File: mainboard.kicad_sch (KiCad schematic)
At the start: 0 parts

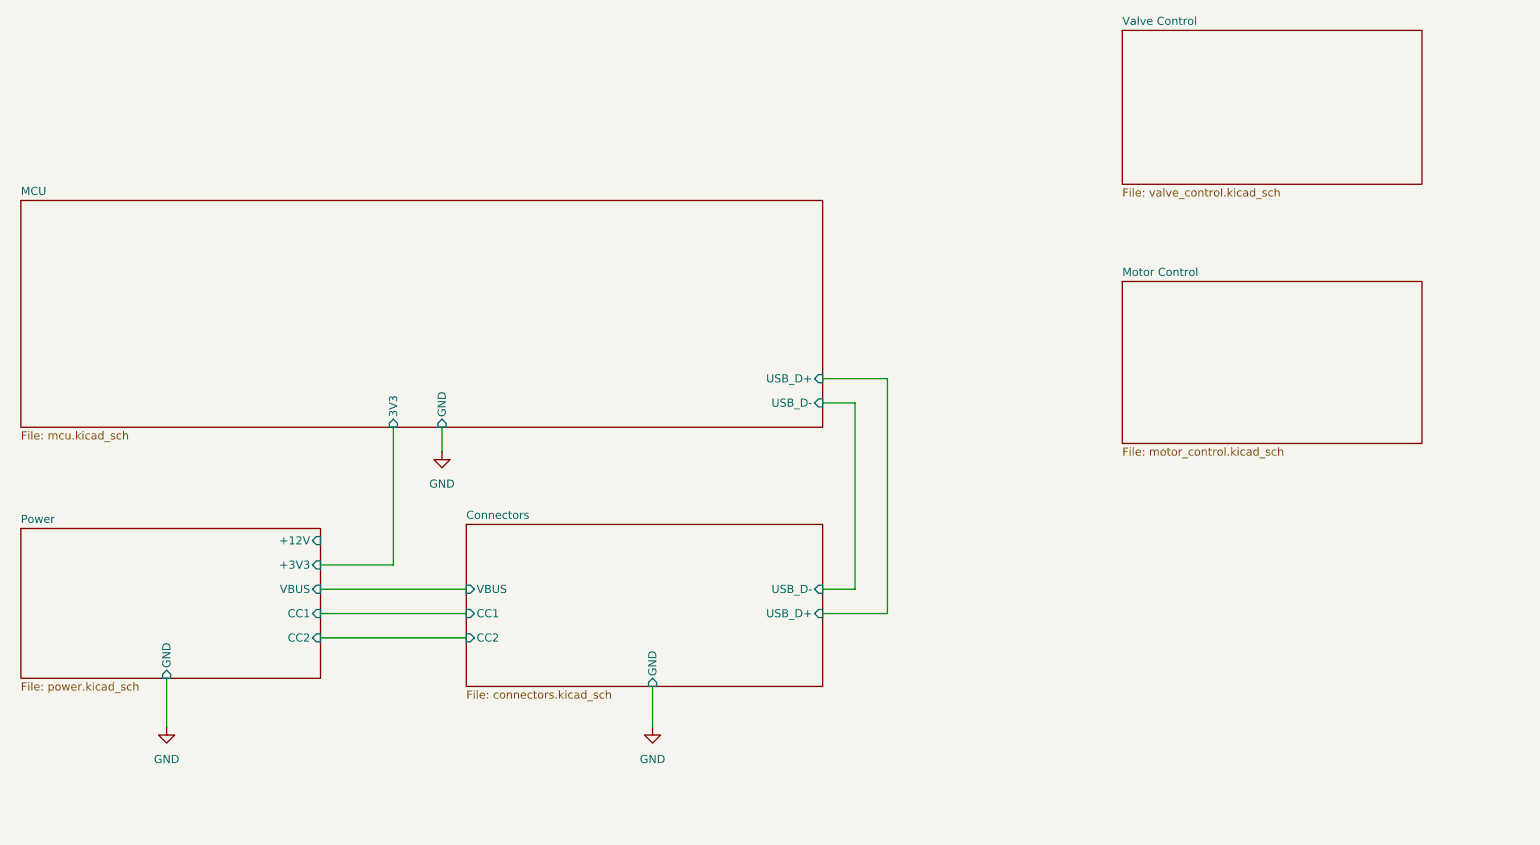
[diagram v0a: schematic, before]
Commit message: Add ESP32-S3-WROOM-1, 5V rail and UI sheet
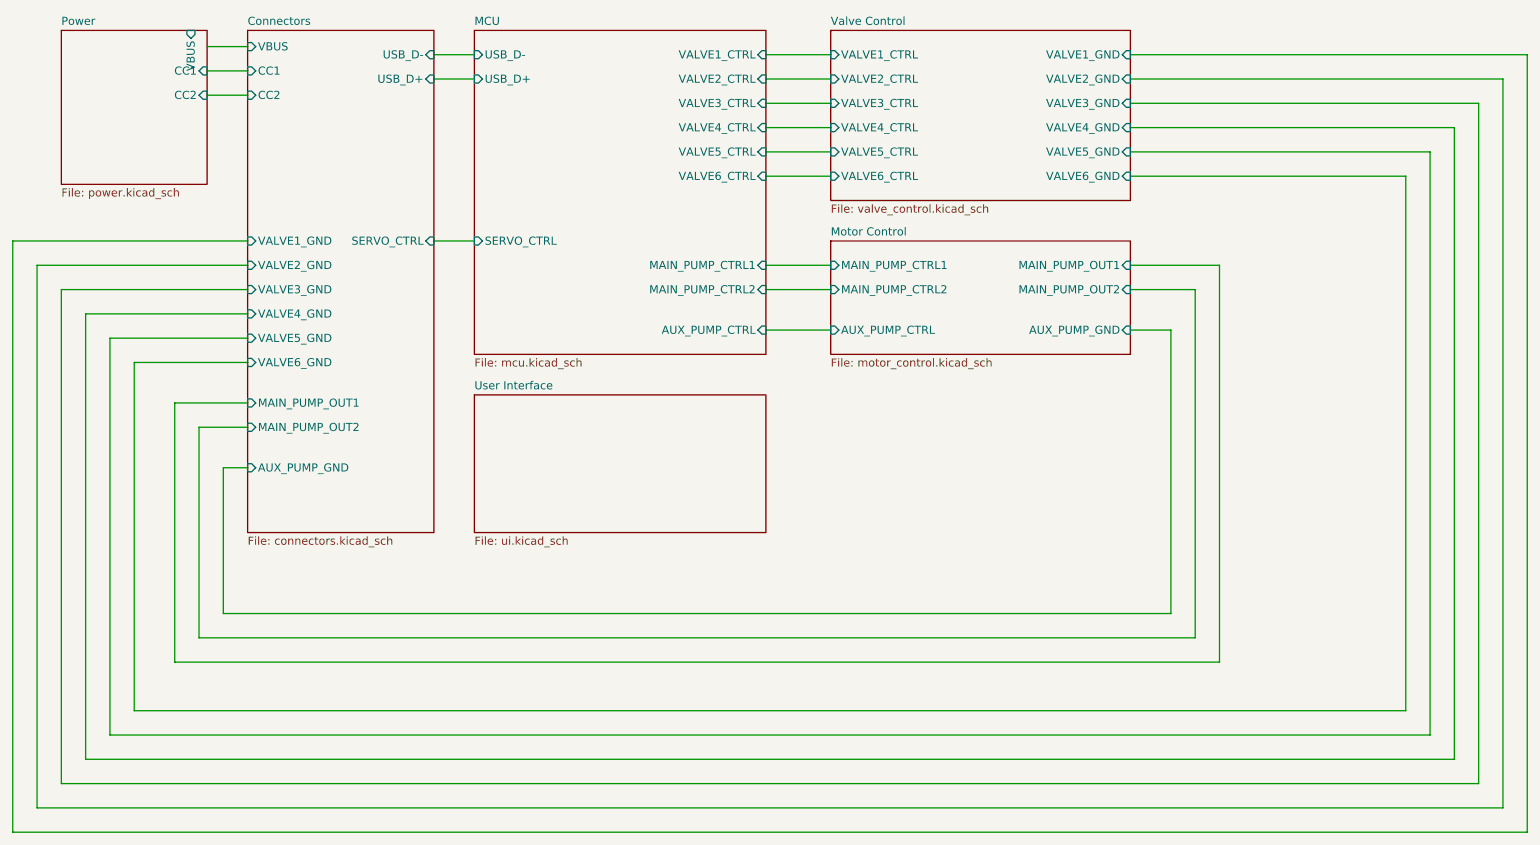
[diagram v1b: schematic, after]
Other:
- added sheet User Interface (ui.kicad_sch)
- sheet Connectors ports: added AUX_PUMP_GND, MAIN_PUMP_OUT1, MAIN_PUMP_OUT2, SERVO_CTRL, VALVE1_GND, VALVE2_GND, VALVE3_GND, VALVE4_GND, VALVE5_GND, VALVE6_GND; removed GND
- sheet MCU ports: added AUX_PUMP_CTRL, MAIN_PUMP_CTRL1, MAIN_PUMP_CTRL2, SERVO_CTRL, VALVE1_CTRL, VALVE2_CTRL, VALVE3_CTRL, VALVE4_CTRL, VALVE5_CTRL, VALVE6_CTRL; removed 3V3, GND
- sheet Motor Control ports: added AUX_PUMP_CTRL, AUX_PUMP_GND, MAIN_PUMP_CTRL1, MAIN_PUMP_CTRL2, MAIN_PUMP_OUT1, MAIN_PUMP_OUT2; removed none
- sheet Power ports: added none; removed +12V, +3V3, GND
- sheet Valve Control ports: added VALVE1_CTRL, VALVE1_GND, VALVE2_CTRL, VALVE2_GND, VALVE3_CTRL, VALVE3_GND, VALVE4_CTRL, VALVE4_GND, VALVE5_CTRL, VALVE5_GND, VALVE6_CTRL, VALVE6_GND; removed none

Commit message: Finish first design
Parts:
- added F1: SF-1206HIA450M-2, Fuse:Fuse_1206_3216Metric, symbol Device:Fuse_Small
- added H1, H2, H3, H4: MountingHole, MountingHole:MountingHole_2.2mm_M2, symbol Mechanical:MountingHole
- added J1: USB_C_Receptacle_USB2.0_16P, project:USB_C_Receptacle_JAE_DX07S016JA1R1500, symbol Connector:USB_C_Receptacle_USB2.0_16P
- added J10: Valve7, Connector_JST:JST_XH_B2B-XH-A_1x02_P2.50mm_Vertical, symbol Connector_Generic:Conn_01x02
- added J11: AuxPump, Connector_JST:JST_XH_B2B-XH-A_1x02_P2.50mm_Vertical, symbol Connector_Generic:Conn_01x02
- added J12: MainPump, Connector_JST:JST_XH_B2B-XH-A_1x02_P2.50mm_Vertical, symbol Connector_Generic:Conn_01x02
- added J13: WaterLevelSensor, Connector_JST:JST_XH_B2B-XH-A_1x02_P2.50mm_Vertical, symbol Connector_Generic:Conn_01x02
- added J14, J15: OneWireTemp, Connector_JST:JST_XH_B3B-XH-A_1x03_P2.50mm_Vertical, symbol Connector_Generic:Conn_01x03
- added J2: Valve1, Connector_JST:JST_XH_B2B-XH-A_1x02_P2.50mm_Vertical, symbol Connector_Generic:Conn_01x02
- added J3: Servo, Connector_JST:JST_XH_B3B-XH-A_1x03_P2.50mm_Vertical, symbol Connector_Generic:Conn_01x03
- added J4: HX711, Connector_JST:JST_XH_B4B-XH-A_1x04_P2.50mm_Vertical, symbol Connector_Generic:Conn_01x04
- added J5: Valve2, Connector_JST:JST_XH_B2B-XH-A_1x02_P2.50mm_Vertical, symbol Connector_Generic:Conn_01x02
- added J6: Valve3, Connector_JST:JST_XH_B2B-XH-A_1x02_P2.50mm_Vertical, symbol Connector_Generic:Conn_01x02
- added J7: Valve4, Connector_JST:JST_XH_B2B-XH-A_1x02_P2.50mm_Vertical, symbol Connector_Generic:Conn_01x02
- added J8: Valve5, Connector_JST:JST_XH_B2B-XH-A_1x02_P2.50mm_Vertical, symbol Connector_Generic:Conn_01x02
- added J9: Valve6, Connector_JST:JST_XH_B2B-XH-A_1x02_P2.50mm_Vertical, symbol Connector_Generic:Conn_01x02
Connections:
- net Power/VBUS: now also F1.2
- new net +15V: J10.1 (Pin_1), J11.1 (Pin_1), J13.1 (Pin_1), J2.1 (Pin_1), J5.1 (Pin_1), J6.1 (Pin_1), J7.1 (Pin_1), J8.1 (Pin_1), J9.1 (Pin_1)
- new net +3.3V: J14.1 (Pin_1), J15.1 (Pin_1)
- new net +5V: J3.1 (Pin_1), J4.1 (Pin_1)
- new net GND: J1.A1 (GND), J1.A12 (GND), J1.B1 (GND), J1.B12 (GND), J1.S1 (SHIELD), J14.3 (Pin_3), J15.3 (Pin_3), J3.3 (Pin_3), J4.4 (Pin_4)
- new net MCU/1WIRE_TEMP: J14.2 (Pin_2), J15.2 (Pin_2)
- new net MCU/HX711_CLK: J4.2 (Pin_2)
- new net MCU/HX711_DAT: J4.3 (Pin_3)
- new net MCU/SERVO_CTRL: J3.2 (Pin_2)
- new net MCU/USB_D+: J1.A6 (D+), J1.B6 (D+)
- new net MCU/USB_D-: J1.A7 (D-), J1.B7 (D-)
- new net MCU/WATER_LEVEL_SENSOR: J13.2 (Pin_2)
- new net Motor Control/AUX_PUMP_GND: J11.2 (Pin_2)
- new net Motor Control/MAIN_PUMP_OUT1: J12.2 (Pin_2)
- new net Motor Control/MAIN_PUMP_OUT2: J12.1 (Pin_1)
- new net Power/CC1: J1.A5 (CC1)
- new net Power/CC2: J1.B5 (CC2)
- new net VBUS_IN: F1.1, J1.A4 (VBUS), J1.A9 (VBUS), J1.B4 (VBUS), J1.B9 (VBUS)
- new net Valve Control/VALVE1_GND: J2.2 (Pin_2)
- new net Valve Control/VALVE2_GND: J5.2 (Pin_2)
- new net Valve Control/VALVE3_GND: J6.2 (Pin_2)
- new net Valve Control/VALVE4_GND: J7.2 (Pin_2)
- new net Valve Control/VALVE5_GND: J8.2 (Pin_2)
- new net Valve Control/VALVE6_GND: J9.2 (Pin_2)
- new net Valve Control/VALVE7_GND: J10.2 (Pin_2)
- no-connect marks 0 -> 2
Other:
- removed sheet Connectors
- sheet MCU ports: added 1WIRE_TEMP, BUTTON_1, BUTTON_2, BUTTON_3, BUZZER, HX711_CLK, HX711_DAT, OLED_SCL, OLED_SDA, PWR_FAULT, VALVE7_CTRL, WATER_LEVEL_SENSOR; removed none
- sheet Motor Control ports: added WATER_LEVEL_SENSOR; removed none
- sheet Power ports: added PWR_FAULT, USB_D+, USB_D-; removed none
- sheet User Interface ports: added BUTTON_1, BUTTON_2, BUTTON_3, BUZZER, OLED_SCL, OLED_SDA; removed none
- sheet Valve Control ports: added VALVE7_GND, VAVLE7_CTRL; removed none
- note added: "Load Cell ADC (HX711) Datasheet: https://cdn.sparkfun.com/datasheets/Sensors/ForceFlex/hx711_english.pdf Current draw: ~ 2mA"
- note added: "Main / Aux. Pump Main pump peak current: ~ 0.6A Aux. pump peak current: ~ 0.7A"
- note added: "Peak Power: -> Two open valve, Main and aux. pump running, Servo active 15V (2 Valves, 2 Pumps): 600 + 600 + 600 + 700 = 3500mA -> 52.5W 5V (Servo, HX711): 800mA + 2mA = 802mA -> 4W 3.3V (MCU): 500mA -> 1.65W Total: 58.15W"
- note added: "Servo Motor Current draw: Idle: 10mA Movement: 120-250mA Stall: 800mA"
- note added: "USB-C PD Connection"
- note added: "Valves Peak current per valve at 15V: ~ 600mA L=21.5mH R=25R"

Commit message: Add reminder to replace fuse
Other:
- note added: "Replace with self-recovery fuse"
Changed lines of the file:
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@@
     (effects (font (size 1.27 1.27)) (justify left bottom))
+  )
+  (text "Replace with self-recovery fuse" (at 88.265 69.85 0)
+    (effects (font (size 1.27 1.27) (color 194 0 0 1)) (justify left bottom))
   )
   (text "Peak Power:\n-> Two open valve, Main and aux. pump running, Servo active\n\n15V (2 Valves, 2 Pumps):\n600 + 600 + 600 + 700 = 3500mA\n-> 52.5W\n\n5V (Servo, HX711):\n800mA + 2mA = 802mA\n-> 4W\n\n3.3V (MCU):\n500mA\n-> 1.65W\n\nTotal: 58.15W"

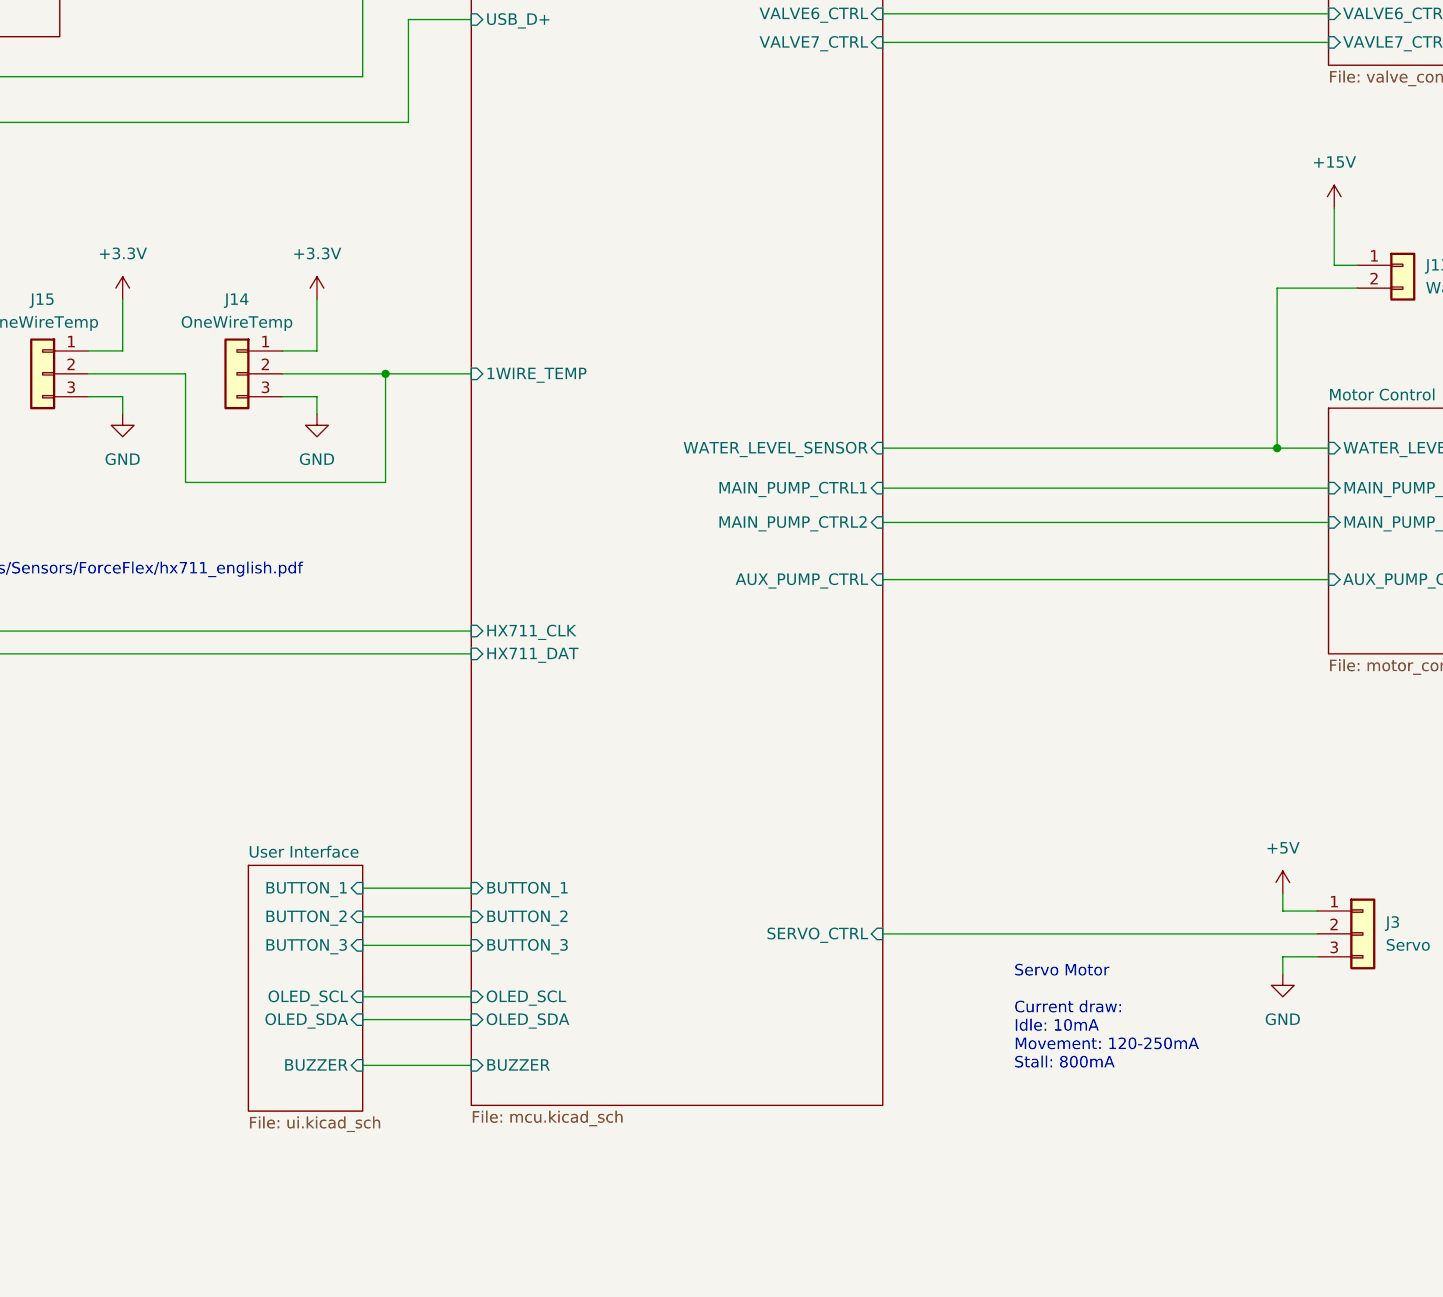
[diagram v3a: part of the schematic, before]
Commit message: Add screen FPC to schematic and remove old OLED stuff
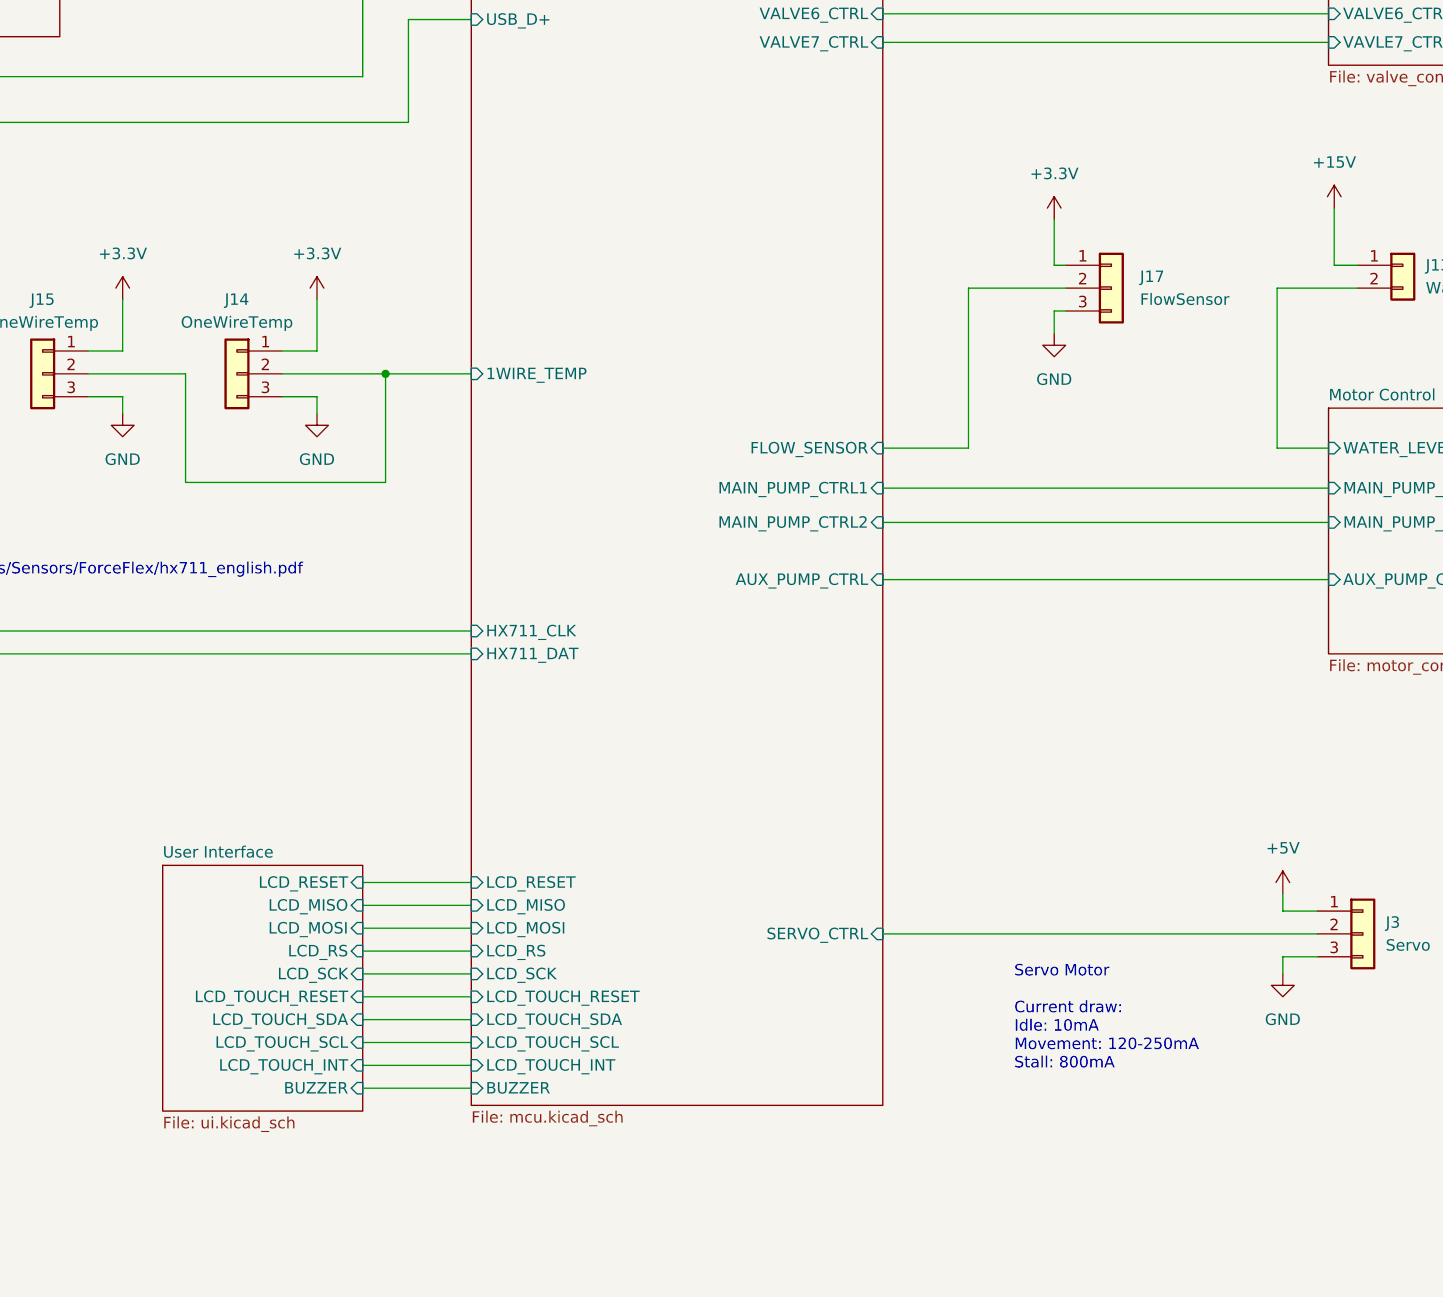
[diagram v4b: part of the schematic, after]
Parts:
- added J17: FlowSensor, Connector_JST:JST_XH_B3B-XH-A_1x03_P2.50mm_Vertical, symbol Connector_Generic:Conn_01x03
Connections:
- net +3.3V: now also J17.1 (Pin_1)
- net GND: now also J17.3 (Pin_3)
- net MCU/WATER_LEVEL_SENSOR renamed Motor Control/WATER_LEVEL_SENSOR
- new net MCU/FLOW_SENSOR: J17.2 (Pin_2)
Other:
- sheet MCU ports: added FLOW_SENSOR, LCD_MISO, LCD_MOSI, LCD_RESET, LCD_RS, LCD_SCK, LCD_TOUCH_INT, LCD_TOUCH_RESET, LCD_TOUCH_SCL, LCD_TOUCH_SDA; removed BUTTON_1, BUTTON_2, BUTTON_3, OLED_SCL, OLED_SDA, WATER_LEVEL_SENSOR
- sheet User Interface ports: added LCD_MISO, LCD_MOSI, LCD_RESET, LCD_RS, LCD_SCK, LCD_TOUCH_INT, LCD_TOUCH_RESET, LCD_TOUCH_SCL, LCD_TOUCH_SDA; removed BUTTON_1, BUTTON_2, BUTTON_3, OLED_SCL, OLED_SDA
